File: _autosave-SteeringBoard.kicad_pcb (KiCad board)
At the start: 2 copper layers, 41.8 x 28 mm, 55 parts, among them J1 SWD, J2 Conn_01x02_Pin, J3 Conn_02x05_Counter_Clockwise, J4 Conn_01x04_Pin, SW1 Reset, U1 STM32L431CBTx, U2 ISO1044BD, U3 CDSOT23-T24CAN, U4 TPS562231DRLR, U5 RO-123.3S

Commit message: finished board with ldo
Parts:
- removed the C12 at (128.6, 92.6)
- removed L1: 3.3uH, Inductor_SMD:L_0603_1608Metric
- removed the R10 at (130.6, 97.6)
- removed the R9 at (130.6, 95.8)
- added C10: 1nF, Capacitor_SMD:C_0603_1608Metric, F.Cu at (130.0, 89.2)
- C11: value 10uF -> 100nF
- U4: value TPS562231DRLR -> TLV70130DBVR; footprint Package_TO_SOT_SMD:SOT-563 -> UTSVT_Power:SOT95P280X145-5N; moved to F.Cu
- moved C11 4.96 mm to (130.2, 94.2)
- moved U4 0.46 mm to (130.5, 91.8), turned to 0 degrees
- renumbered C13 to C12, C14 to C13, C15 to C14, C5 to C4, C6 to C5, C7 to C6, C8 to C7, C9 to C8, C10 to C9, R12 to R10, R11 to R9
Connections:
- C11 pad 1: /12V_Ext -> +12V
- U4 pad 1: /12V_Ext -> /3V3_Bus
- U4 pad 2: /PowerDist/SW -> GNDPWR
- U4 pad 3: GNDPWR -> +12V
- U4 pad 4: /PowerDist/BST -> unconnected-(U4-NC-Pad4)
- U4 pad 5: /12V_Ext -> unconnected-(U4-NC-Pad5)
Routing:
- net /PowerDist/FB: track 16.1 -> 0.00 mm, vias 1 -> 0
- net GNDPWR: track 19.8 -> 31.6 mm, vias 5 -> 3
- net /PowerDist/SW: track 10.9 -> 0.00 mm, vias 1 -> 0
- net /3V3_Bus: track 20.3 -> 11.2 mm, vias 3 -> 2
- net /12V_Ext: track 1.71 -> 0.00 mm
- net /PowerDist/BST: track 1.60 -> 0.00 mm, vias 1 -> 0
- net Net-(D7-A): track 11.6 -> 12.9 mm
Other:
- board size 41.8 x 28 mm -> 42.7 x 24.7 mm

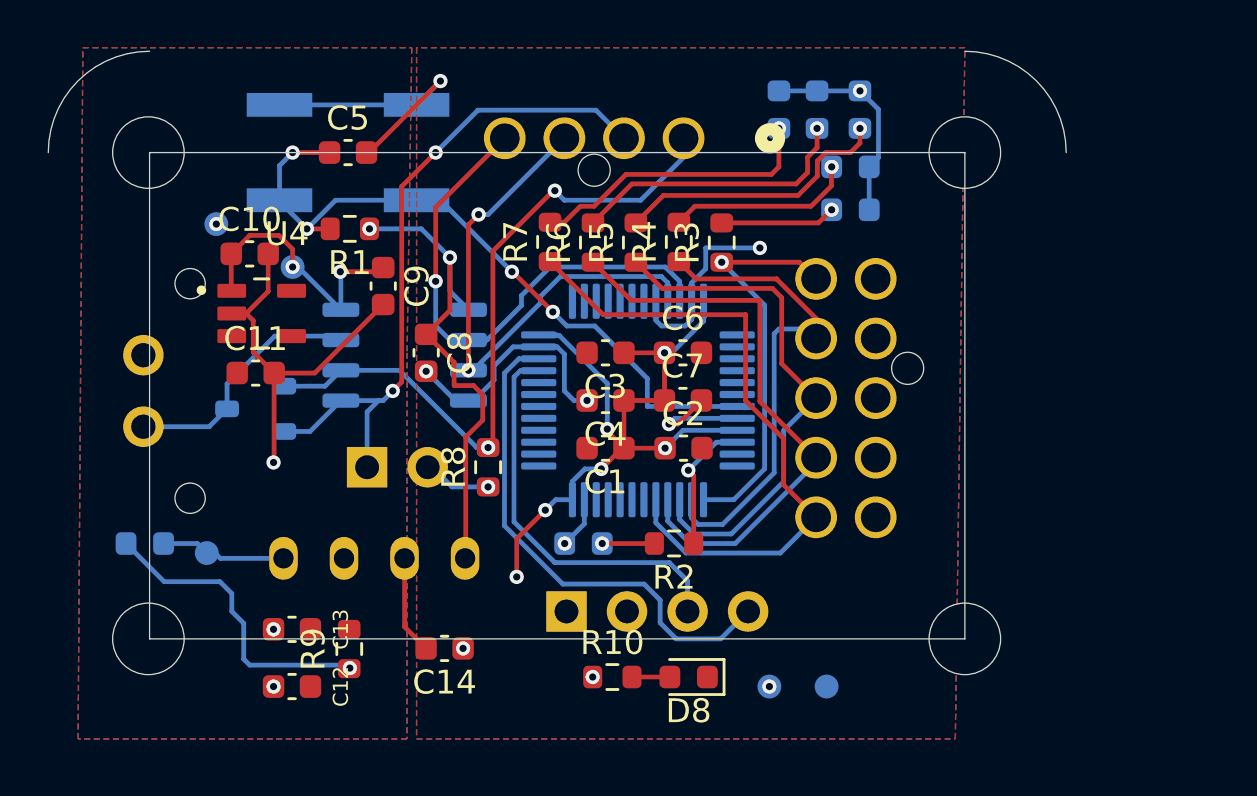
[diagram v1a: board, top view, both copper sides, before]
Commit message: finished board with bad edgecuts
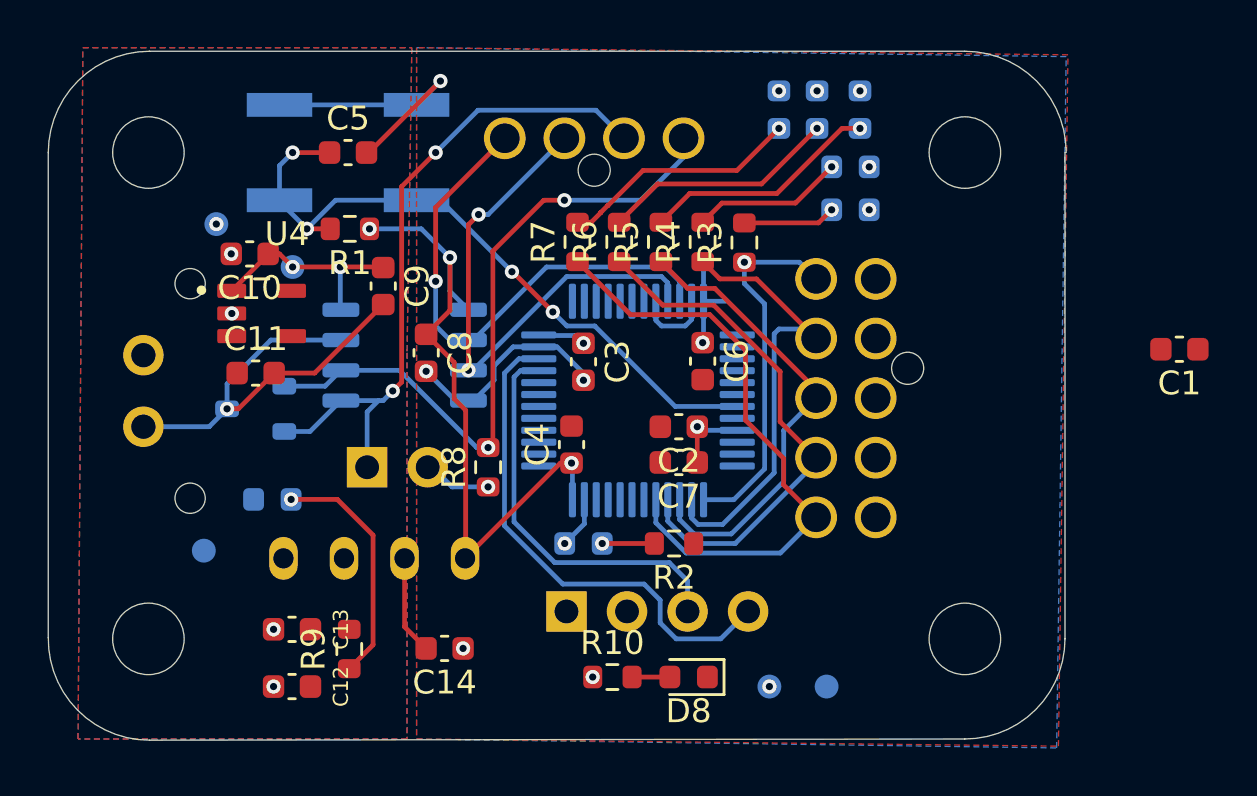
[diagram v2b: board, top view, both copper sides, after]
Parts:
- moved C1 24.4 mm to (169.0, 93.2)
- moved D7 5.66 mm to (130.9, 99.5), turned to 0 degrees
- moved C7 2.61 mm to (148.0, 98.0), turned to 180 degrees
- moved C4 2.34 mm to (143.5, 97.2), turned to 90 degrees
- moved R7 1.15 mm to (143.8, 88.8)
- moved R6 1.10 mm to (145.5, 88.8)
- moved R5 1.05 mm to (147.2, 88.8)
- moved R4 1.00 mm to (149.0, 88.8)
- moved C3 1.00 mm to (144.0, 93.8), turned to -90 degrees
- moved R3 0.95 mm to (150.8, 88.8)
- moved C2 0.92 mm to (148.0, 96.5), turned to 180 degrees
- moved C6 0.90 mm to (149.0, 93.8), turned to -90 degrees
- moved TP2 0.16 mm to (128.1, 101.7)
- turned C10 to 180 degrees
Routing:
- net GND: track 49.0 -> 29.4 mm, vias 8 -> 10
- net +3.3V: track 51.4 -> 36.2 mm, vias 10 -> 8
- net GNDPWR: track 31.6 -> 18.8 mm, vias 3 -> 5
- net /PA0: track 5.70 -> 0.00 mm, vias 1 -> 0
- net Net-(D7-A): track 12.9 -> 10.1 mm
- net /REG-: track 22.0 -> 19.5 mm
- net /TSS-: track 24.2 -> 21.8 mm
- net /3V3_Bus: track 11.2 -> 9.08 mm
- net Net-(D6-A): track 12.2 -> 10.1 mm
- net /HRN_PD-: track 27.7 -> 25.7 mm
- net Net-(D5-A): track 11.9 -> 9.93 mm
- net Net-(D4-A): track 11.8 -> 9.98 mm
- net /CRS_SET-: track 20.1 -> 18.6 mm
- net Net-(D3-A): track 7.84 -> 6.38 mm
- net /RGEN_E-: track 16.8 -> 15.4 mm
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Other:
- board size 42.7 x 24.7 mm -> 42.7 x 28.9 mm
